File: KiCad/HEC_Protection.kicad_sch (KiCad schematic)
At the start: 19 parts, among them U11 74LS00, U11 74LS32, U12 74LS04, U16 74LS32, U17 74LS74, U18 74LS138, U18 74LS74, U19 74LS30, U22 74LS02, U23 74LS74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

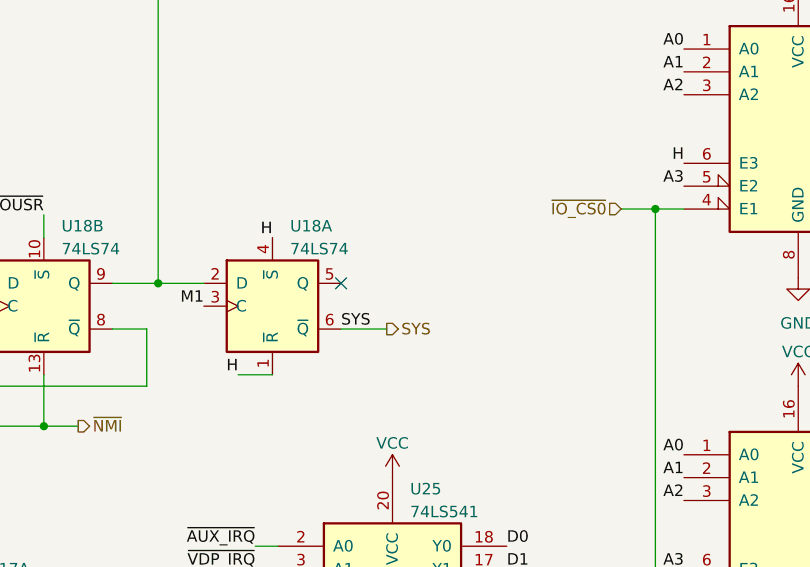
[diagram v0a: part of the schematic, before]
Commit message: Change LED display type
Changed LED display to include two decimal points to indicate usr/sys mode. This type of LED display is easier to source.
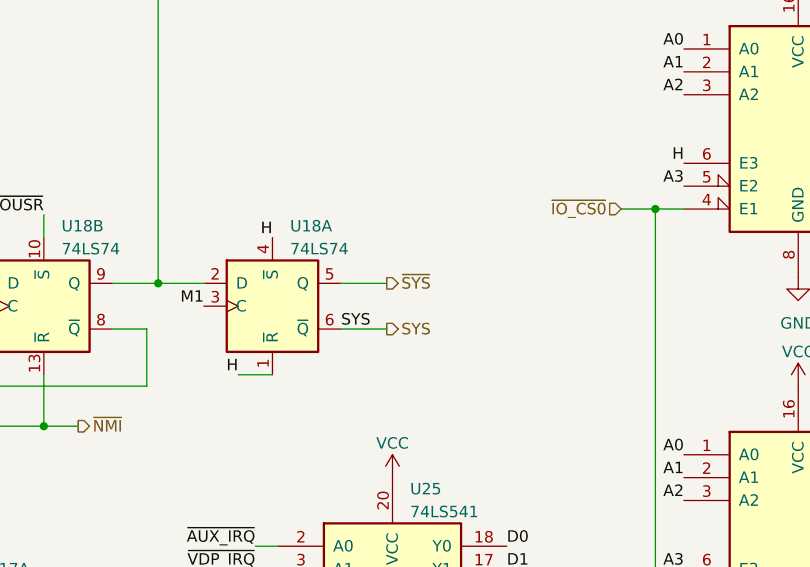
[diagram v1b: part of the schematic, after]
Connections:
- net ~{SYS}: now reaches U18.5 (Q)
- no-connect marks 16 -> 15
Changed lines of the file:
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@@
   )
   (no_connect (at 262.89 85.09))
-  (no_connect (at 199.39 53.34))
   (no_connect (at 166.37 140.97))
   (no_connect (at 40.005 36.195))
@@
     (stroke (width 0) (type default))
   )
+  (wire (pts (xy 199.39 53.34) (xy 204.47 53.34))
+    (stroke (width 0) (type default))
+  )
   (wire (pts (xy 76.835 66.675) (xy 81.915 66.675))
     (stroke (width 0) (type default))
@@
     (effects (font (size 1.27 1.27)) (justify right))
   )
+  (hierarchical_label "~{SYS}" (shape output) (at 204.47 53.34 0) (fields_autoplaced)
+    (effects (font (size 1.27 1.27)) (justify left))
+  )
   (hierarchical_label "A[0..3]" (shape input) (at 22.225 106.68 180) (fields_autoplaced)

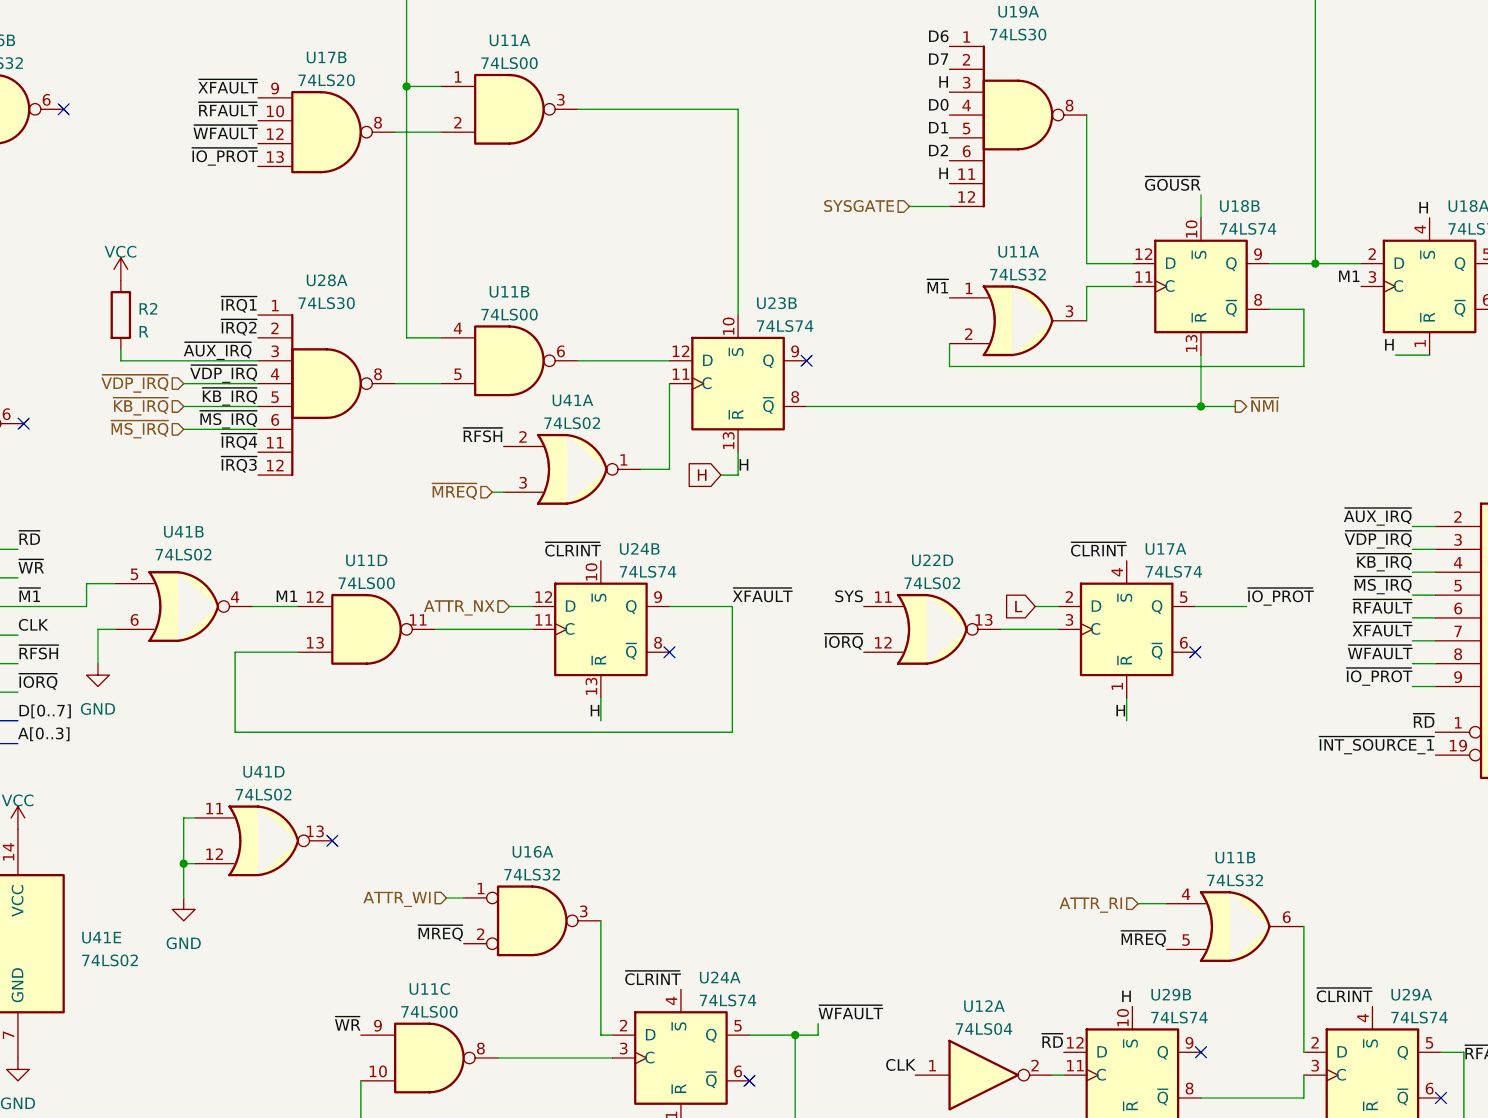
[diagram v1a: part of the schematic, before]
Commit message: change NX bit to XE bit
change No eXecute to eXecute Enable (inverting the polarity of the signal) in order to fix a bug that causes the HEC to not recognize a NX when the instruction fetched is a RST.
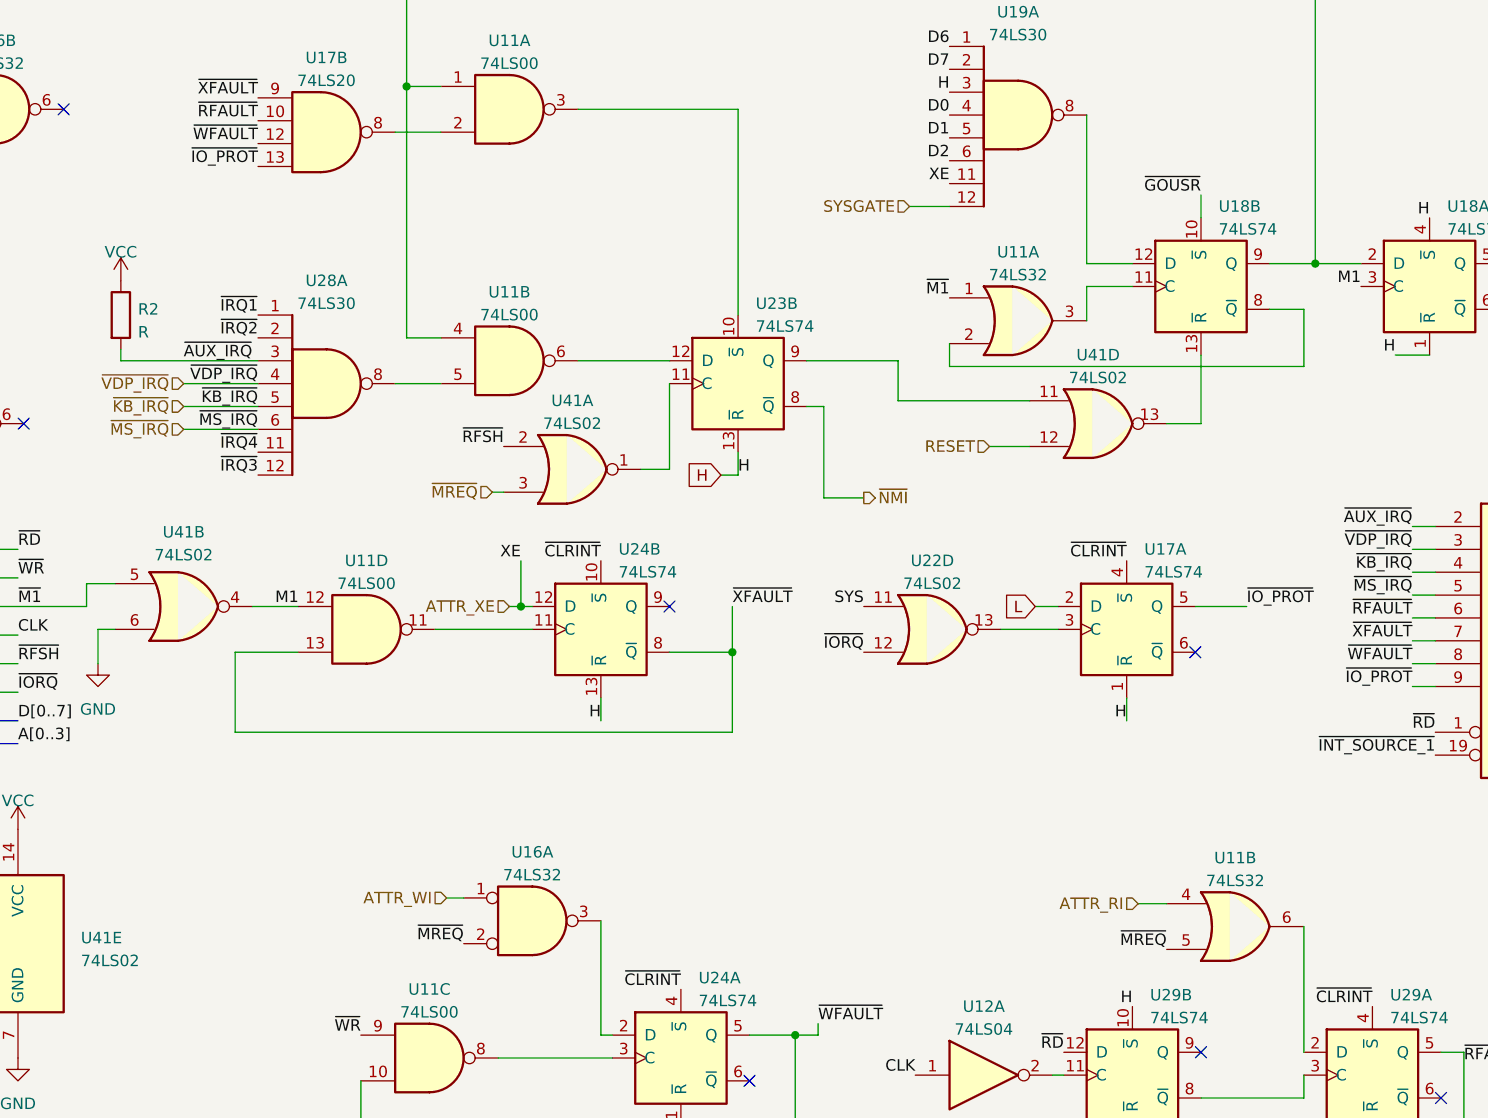
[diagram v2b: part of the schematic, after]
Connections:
- net GND: no longer U41.11, U41.12
- net H: no longer U19.11
- net ~{NMI}: no longer U18.13 (~{R})
- net ~{XFAULT}: now also U24.8 (~{Q}); no longer U24.9 (Q)
- net at U41.13: now also U18.13 (~{R})
- net at U23.9 (Q): now also U41.11
- net ATTR_NX renamed ATTR_XE
- net ATTR_XE: now also U19.11
- new net RESET: U41.12
- no-connect marks 15 -> 13
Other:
- moved on the sheet: U41D
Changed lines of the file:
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@@
   (junction (at 78.105 33.655) (diameter 0) (color 0 0 0 0)
   )
+  (junction (at 90.805 91.44) (diameter 0) (color 0 0 0 0)
+  )
+  (junction (at 114.3 96.52) (diameter 0) (color 0 0 0 0)
+  )
   (junction (at 234.315 45.085) (diameter 0) (color 0 0 0 0)
   )
-  (junction (at 53.34 120.015) (diameter 0) (color 0 0 0 0)
-  )
   (junction (at 23.495 38.735) (diameter 0) (color 0 0 0 0)
   )
@@
   )
   (junction (at 179.07 53.34) (diameter 0) (color 0 0 0 0)
-  )
-  (junction (at 166.37 69.215) (diameter 0) (color 0 0 0 0)
   )
   (no_connect (at 262.89 85.09))
@@
   (no_connect (at 40.005 36.195))
   (no_connect (at 262.89 90.17))
-  (no_connect (at 69.85 117.475))
   (no_connect (at 165.735 96.52))
   (no_connect (at 116.205 144.145))
   (no_connect (at 262.89 80.01))
-  (no_connect (at 122.555 64.135))
   (no_connect (at 262.89 87.63))
   (no_connect (at 193.04 146.05))
   (no_connect (at 35.56 71.12))
-  (no_connect (at 107.315 96.52))
+  (no_connect (at 107.315 91.44))
   (no_connect (at 262.89 82.55))
   (no_connect (at 262.89 77.47))
@@
     (stroke (width 0) (type default))
   )
-  (wire (pts (xy 166.37 69.215) (xy 166.37 63.5))
-    (stroke (width 0) (type default))
-  )
   (wire (pts (xy 234.315 90.17) (xy 237.49 90.17))
     (stroke (width 0) (type default))
@@
     (stroke (width 0) (type default))
   )
+  (wire (pts (xy 142.875 73.66) (xy 147.32 73.66))
+    (stroke (width 0) (type default))
+  )
   (wire (pts (xy 247.015 136.525) (xy 254.635 136.525))
     (stroke (width 0) (type default))
@@
     (stroke (width 0) (type default))
   )
+  (wire (pts (xy 124.46 79.375) (xy 124.46 69.215))
+    (stroke (width 0) (type default))
+  )
   (wire (pts (xy 153.67 36.83) (xy 153.67 53.34))
     (stroke (width 0) (type default))
@@
     (stroke (width 0) (type default))
   )
-  (wire (pts (xy 89.535 91.44) (xy 92.075 91.44))
+  (wire (pts (xy 89.535 91.44) (xy 90.805 91.44))
     (stroke (width 0) (type default))
   )
@@
     (stroke (width 0) (type default))
   )
-  (wire (pts (xy 53.34 120.015) (xy 54.61 120.015))
-    (stroke (width 0) (type default))
-  )
   (bus (pts (xy 244.475 128.905) (xy 244.475 131.445))
     (stroke (width 0) (type default))
@@
     (stroke (width 0) (type default))
   )
-  (wire (pts (xy 166.37 69.215) (xy 170.18 69.215))
+  (wire (pts (xy 162.56 71.12) (xy 166.37 71.12))
+    (stroke (width 0) (type default))
+  )
+  (wire (pts (xy 90.805 91.44) (xy 92.075 91.44))
+    (stroke (width 0) (type default))
+  )
+  (wire (pts (xy 124.46 79.375) (xy 128.905 79.375))
     (stroke (width 0) (type default))
   )
@@
     (stroke (width 0) (type default))
   )
-  (wire (pts (xy 53.34 114.935) (xy 53.34 120.015))
-    (stroke (width 0) (type default))
-  )
   (wire (pts (xy 262.89 29.845) (xy 274.955 29.845))
     (stroke (width 0) (type default))
@@
     (stroke (width 0) (type default))
   )
+  (wire (pts (xy 90.805 86.36) (xy 90.805 91.44))
+    (stroke (width 0) (type default))
+  )
   (wire (pts (xy 234.315 45.085) (xy 237.49 45.085))
     (stroke (width 0) (type default))
@@
     (stroke (width 0) (type default))
   )
-  (wire (pts (xy 122.555 69.215) (xy 166.37 69.215))
+  (wire (pts (xy 122.555 69.215) (xy 124.46 69.215))
     (stroke (width 0) (type default))
   )
@@
     (stroke (width 0) (type default))
   )
+  (wire (pts (xy 166.37 63.5) (xy 166.37 71.12))
+    (stroke (width 0) (type default))
+  )
   (wire (pts (xy 247.015 128.905) (xy 254.635 128.905))
     (stroke (width 0) (type default))
@@
     (stroke (width 0) (type default))
   )
+  (wire (pts (xy 122.555 64.135) (xy 132.715 64.135))
+    (stroke (width 0) (type default))
+  )
   (wire (pts (xy 23.495 33.655) (xy 24.765 33.655))
     (stroke (width 0) (type default))
@@
     (stroke (width 0) (type default))
   )
+  (wire (pts (xy 132.715 68.58) (xy 147.32 68.58))
+    (stroke (width 0) (type default))
+  )
+  (wire (pts (xy 132.715 64.135) (xy 132.715 68.58))
+    (stroke (width 0) (type default))
+  )
   (wire (pts (xy 23.495 33.655) (xy 23.495 38.735))
     (stroke (width 0) (type default))
   )
-  (wire (pts (xy 107.315 91.44) (xy 114.3 91.44))
-    (stroke (width 0) (type default))
-  )
   (wire (pts (xy 247.015 123.825) (xy 254.635 123.825))
     (stroke (width 0) (type default))
@@
     (stroke (width 0) (type default))
   )
+  (wire (pts (xy 107.315 96.52) (xy 114.3 96.52))
+    (stroke (width 0) (type default))
+  )
   (wire (pts (xy 262.89 42.545) (xy 274.955 42.545))
     (stroke (width 0) (type default))
@@
     (stroke (width 0) (type default))
   )
-  (wire (pts (xy 53.34 120.015) (xy 53.34 123.825))
+  (wire (pts (xy 114.3 96.52) (xy 114.3 105.41))
     (stroke (width 0) (type default))
   )
@@
     (stroke (width 0) (type default))
   )
-  (wire (pts (xy 54.61 114.935) (xy 53.34 114.935))
-    (stroke (width 0) (type default))
-  )
   (wire (pts (xy 158.75 55.88) (xy 153.67 55.88))
     (stroke (width 0) (type default))
@@
     (stroke (width 0) (type default))
   )
-  (wire (pts (xy 114.3 91.44) (xy 114.3 105.41))
+  (wire (pts (xy 114.3 91.44) (xy 114.3 96.52))
     (stroke (width 0) (type default))
   )
@@
     (effects (font (size 1.27 1.27)) (justify right bottom))
   )
+  (label "XE" (at 90.805 86.36 180) (fields_autoplaced)
+    (effects (font (size 1.27 1.27)) (justify right bottom))
+  )
   (label "~{IO_PROT}" (at 171.45 91.44 0) (fields_autoplaced)
     (effects (font (size 1.27 1.27)) (justify left bottom))
@@
     (effects (font (size 1.27 1.27)) (justify right bottom))
   )
-  (label "H" (at 138.43 44.45 180) (fields_autoplaced)
-    (effects (font (size 1.27 1.27)) (justify right bottom))
-  )
   (label "~{RD}" (at 151.13 140.97 180) (fields_autoplaced)
     (effects (font (size 1.27 1.27)) (justify right bottom))
@@
   (label "D7" (at 280.035 139.065 0) (fields_autoplaced)
     (effects (font (size 1.27 1.27)) (justify left bottom))
+  )
+  (label "XE" (at 138.43 44.45 180) (fields_autoplaced)
+    (effects (font (size 1.27 1.27)) (justify right bottom))
   )
   (label "~{IRQ4}" (at 61.595 74.295 180) (fields_autoplaced)
@@
     (effects (font (size 1.27 1.27)) (justify right))
   )
+  (hierarchical_label "RESET" (shape input) (at 142.875 73.66 180) (fields_autoplaced)
+    (effects (font (size 1.27 1.27)) (justify right))
+  )
   (hierarchical_label "~{WR}" (shape input) (at 22.225 88.265 180) (fields_autoplaced)
     (effects (font (size 1.27 1.27)) (justify right))
@@
     (effects (font (size 1.27 1.27)) (justify right))
   )
-  (hierarchical_label "ATTR_NX" (shape input) (at 89.535 91.44 180) (fields_autoplaced)
+  (hierarchical_label "ATTR_XE" (shape input) (at 89.535 91.44 180) (fields_autoplaced)
     (effects (font (size 1.27 1.27)) (justify right))
   )
@@
     (effects (font (size 1.27 1.27)) (justify right))
   )
-  (hierarchical_label "~{NMI}" (shape output) (at 170.18 69.215 0) (fields_autoplaced)
+  (hierarchical_label "~{NMI}" (shape output) (at 128.905 79.375 0) (fields_autoplaced)
     (effects (font (size 1.27 1.27)) (justify left))
   )
@@
     )
   )
-  (symbol (lib_id "74xx:74LS02") (at 62.23 117.475 0) (unit 4)
-    (in_bom yes) (on_board yes) (dnp no) (fields_autoplaced)
-    (property "Reference" "U41" (at 62.23 109.855 0)
-      (effects (font (size 1.27 1.27)))
-    )
-    (property "Value" "74LS02" (at 62.23 112.395 0)
-      (effects (font (size 1.27 1.27)))
-    )
-    (property "Footprint" "Library:DIP-14_W7.62mm_Socket_ThinPads" (at 62.23 117.475 0)
-      (effects (font (size 1.27 1.27)) hide)
-    )
-    (property "Datasheet" "http://www.ti.com/lit/gpn/sn74ls02" (at 62.23 117.475 0)
+  (symbol (lib_id "74xx:74LS02") (at 154.94 71.12 0) (unit 4)
+    (in_bom yes) (on_board yes) (dnp no) (fields_autoplaced)
+    (property "Reference" "U41" (at 154.94 63.5 0)
+      (effects (font (size 1.27 1.27)))
+    )
+    (property "Value" "74LS02" (at 154.94 66.04 0)
+      (effects (font (size 1.27 1.27)))
+    )
+    (property "Footprint" "Library:DIP-14_W7.62mm_Socket_ThinPads" (at 154.94 71.12 0)
+      (effects (font (size 1.27 1.27)) hide)
+    )
+    (property "Datasheet" "http://www.ti.com/lit/gpn/sn74ls02" (at 154.94 71.12 0)
       (effects (font (size 1.27 1.27)) hide)
     )
@@
         )
       )
-    )
-  )
-  (symbol (lib_id "power:GND") (at 53.34 123.825 0) (unit 1)
-    (in_bom yes) (on_board yes) (dnp no) (fields_autoplaced)
-    (property "Reference" "#PWR0106" (at 53.34 130.175 0)
-      (effects (font (size 1.27 1.27)) hide)
-    )
-    (property "Value" "GND" (at 53.34 128.905 0)
-      (effects (font (size 1.27 1.27)))
-    )
-    (property "Footprint" "" (at 53.34 123.825 0)
-      (effects (font (size 1.27 1.27)) hide)
-    )
-    (property "Datasheet" "" (at 53.34 123.825 0)
-      (effects (font (size 1.27 1.27)) hide)
-    )
-    (pin "1")
-    (instances
-      (project "HEC1"
-        (path "/87935374-b60a-4f41-99da-94b76103dd77"
-          (reference "#PWR0106") (unit 1)
-        )
-        (path "/87935374-b60a-4f41-99da-94b76103dd77/2930b625-d6a3-4a7f-9d41-a454efcef99d"
-          (reference "#PWR0106") (unit 1)
-        )
-      )
